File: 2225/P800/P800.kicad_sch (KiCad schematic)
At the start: 25 parts, among them J1 Screw_Terminal_01x04, J2 Screw_Terminal_01x08

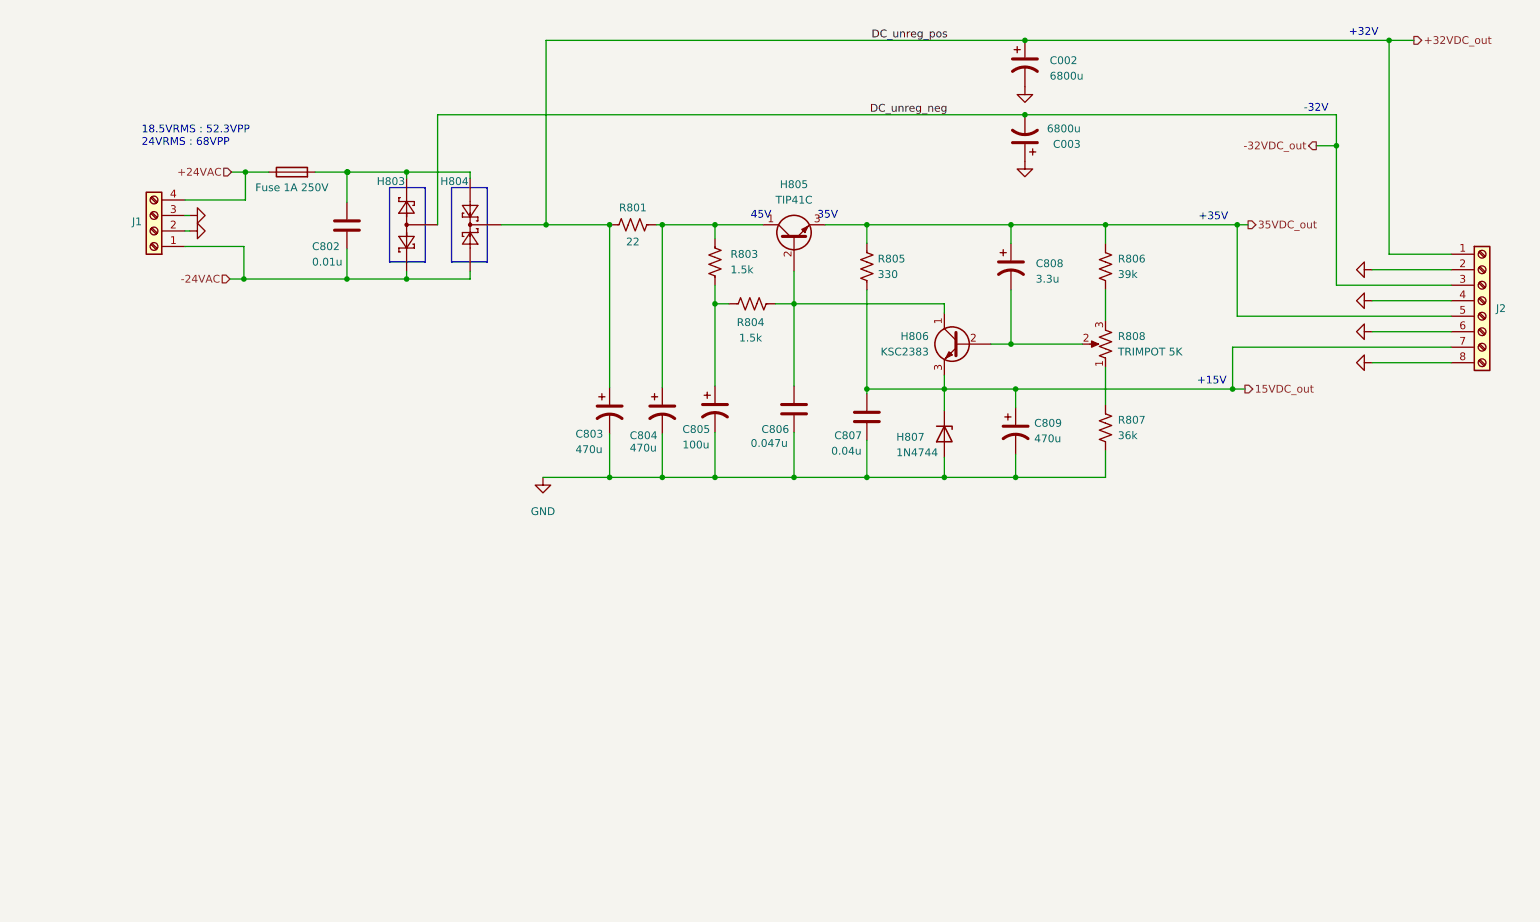
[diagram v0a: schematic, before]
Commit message: Connected transformer to P800 in 2225.kicad_sch; changed transformer model resistances in 2225.lib
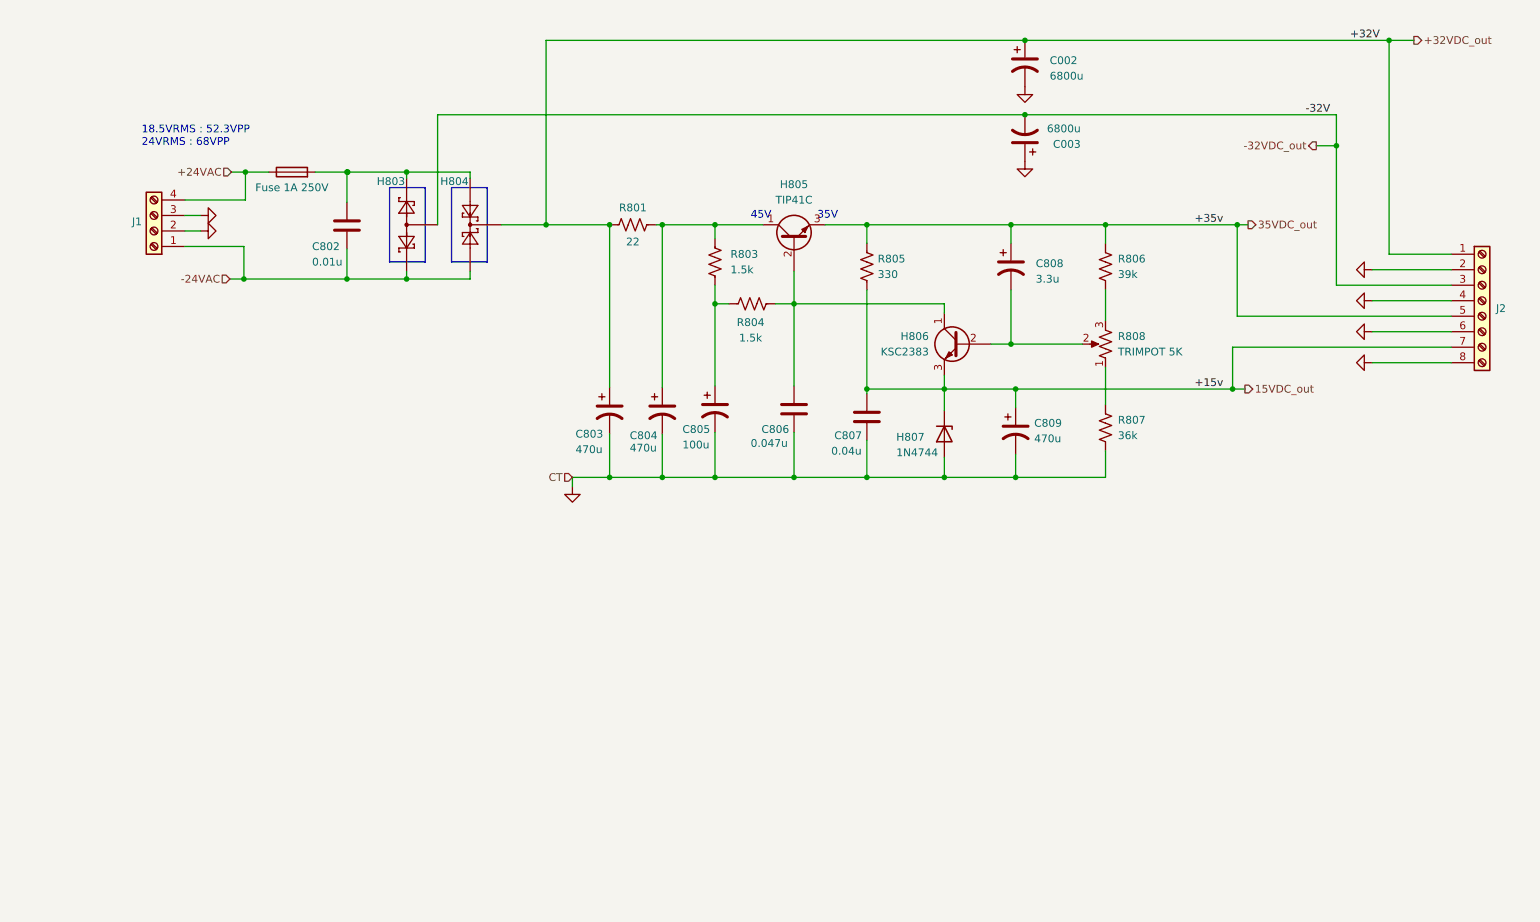
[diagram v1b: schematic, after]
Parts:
- J1: Spice_Model (none) -> Screw_Terminal_01x04; Spice_Netlist_Enabled (none) -> N; Spice_Primitive (none) -> J
- J2: Spice_Model (none) -> Screw_Terminal_01x08; Spice_Netlist_Enabled (none) -> N; Spice_Primitive (none) -> J
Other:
- note removed: "+15V"
- note removed: "+32V"
- note removed: "+35V"
- note removed: "-32V"
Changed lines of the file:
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@@
-    (stroke (width 0) (type default) (color 0 0 0 0))
-  )
-  (wire (pts (xy 102.362 125.222) (xy 113.284 125.222))
     (stroke (width 0) (type default) (color 0 0 0 0))
   )
@@
     (stroke (width 0) (type default) (color 0 0 0 0))
   )
-  (wire (pts (xy 44.45 84.836) (xy 43.688 84.836))
-    (stroke (width 0) (type default) (color 0 0 0 0))
-  )
   (polyline (pts (xy 83.058 77.724) (xy 83.058 89.916))
     (stroke (width 0) (type default) (color 0 0 0 0))
@@
     (stroke (width 0) (type default) (color 0 0 0 0))
   )
+  (wire (pts (xy 107.188 126.746) (xy 107.188 125.222))
+    (stroke (width 0) (type default) (color 0 0 0 0))
+  )
   (polyline (pts (xy 77.216 77.724) (xy 83.058 77.724))
     (stroke (width 0) (type default) (color 0 0 0 0))
@@
     (stroke (width 0) (type default) (color 0 0 0 0))
   )
-  (wire (pts (xy 44.45 82.296) (xy 43.688 82.296))
-    (stroke (width 0) (type default) (color 0 0 0 0))
-  )
   (wire (pts (xy 168.148 108.458) (xy 168.148 110.744))
     (stroke (width 0) (type default) (color 0 0 0 0))
@@
     (stroke (width 0) (type default) (color 0 0 0 0))
   )
+  (wire (pts (xy 46.228 84.836) (xy 43.688 84.836))
+    (stroke (width 0) (type default) (color 0 0 0 0))
+  )
   (wire (pts (xy 80.01 76.2) (xy 80.01 75.184))
     (stroke (width 0) (type default) (color 0 0 0 0))
@@
     (stroke (width 0) (type default) (color 0 0 0 0))
   )
+  (wire (pts (xy 43.688 82.296) (xy 46.228 82.296))
+    (stroke (width 0) (type default) (color 0 0 0 0))
+  )
   (wire (pts (xy 251.206 96.266) (xy 238.252 96.266))
     (stroke (width 0) (type default) (color 0 0 0 0))
@@
   )
   (wire (pts (xy 121.92 125.222) (xy 113.284 125.222))
+    (stroke (width 0) (type default) (color 0 0 0 0))
+  )
+  (wire (pts (xy 107.188 125.222) (xy 113.284 125.222))
     (stroke (width 0) (type default) (color 0 0 0 0))
   )
@@
     (effects (font (size 1.27 1.27)) (justify left bottom))
   )
-  (text "+15V" (at 209.55 110.236 0)
-    (effects (font (size 1.27 1.27)) (justify left bottom))
-  )
-  (text "+35V" (at 209.804 83.312 0)
-    (effects (font (size 1.27 1.27)) (justify left bottom))
-  )
   (text "35V" (at 147.32 83.058 0)
     (effects (font (size 1.27 1.27)) (justify left bottom))
   )
-  (text "-32V" (at 227.076 65.532 0)
-    (effects (font (size 1.27 1.27)) (justify left bottom))
-  )
-  (text "+32V" (at 234.442 53.086 0)
-    (effects (font (size 1.27 1.27)) (justify left bottom))
-  )
-  (label "DC_unreg_neg" (at 155.956 65.786 0)
-    (effects (font (size 1.27 1.27)) (justify left bottom))
-  )
-  (label "DC_unreg_pos" (at 156.21 53.594 0)
-    (effects (font (size 1.27 1.27)) (justify left bottom))
+  (label "+35v" (at 213.868 83.82 180)
+    (effects (font (size 1.27 1.27)) (justify right bottom))
+  )
+  (label "-32V" (at 231.394 65.786 180)
+    (effects (font (size 1.27 1.27)) (justify right bottom))
+  )
+  (label "+32V" (at 239.522 53.594 180)
+    (effects (font (size 1.27 1.27)) (justify right bottom))
+  )
+  (label "+15v" (at 213.868 110.744 180)
+    (effects (font (size 1.27 1.27)) (justify right bottom))
   )
   (hierarchical_label "35VDC_out" (shape output) (at 217.932 83.82 0)
     (effects (font (size 1.27 1.27)) (justify left))
   )
+  (hierarchical_label "CT" (shape input) (at 107.188 125.222 180)
+    (effects (font (size 1.27 1.27)) (justify right))
+  )
   (hierarchical_label "-24VAC" (shape input) (at 51.054 92.71 180)
     (effects (font (size 1.27 1.27)) (justify right))
@@
     (pin "2")
   )
-  (symbol (lib_id "power:GND") (at 44.45 82.296 90) (unit 1)
-    (in_bom yes) (on_board yes) (fields_autoplaced)
-    (property "Reference" "#PWR?" (id 0) (at 50.8 82.296 0)
-      (effects (font (size 1.27 1.27)) hide)
-    )
-    (property "Value" "GND" (id 1) (at 47.752 82.2959 90)
-      (effects (font (size 1.27 1.27)) (justify right) hide)
-    )
-    (property "Footprint" "" (id 2) (at 44.45 82.296 0)
-      (effects (font (size 1.27 1.27)) hide)
-    )
-    (property "Datasheet" "" (id 3) (at 44.45 82.296 0)
-      (effects (font (size 1.27 1.27)) hide)
-    )
-    (pin "1")
-  )
   (symbol (lib_id "Device:R_US") (at 194.564 90.678 180) (unit 1)
     (in_bom yes) (on_board yes) (fields_autoplaced)
@@
     )
     (property "Datasheet" "~" (id 3) (at 256.286 96.266 0)
+      (effects (font (size 1.27 1.27)) hide)
+    )
+    (property "Spice_Primitive" "J" (id 4) (at 256.286 96.266 0)
+      (effects (font (size 1.27 1.27)) hide)
+    )
+    (property "Spice_Model" "Screw_Terminal_01x08" (id 5) (at 256.286 96.266 0)
+      (effects (font (size 1.27 1.27)) hide)
+    )
+    (property "Spice_Netlist_Enabled" "N" (id 6) (at 256.286 96.266 0)
       (effects (font (size 1.27 1.27)) hide)
     )
@@
     (pin "8")
   )
-  (symbol (lib_id "power:GND") (at 102.362 125.222 0) (unit 1)
-    (in_bom yes) (on_board yes) (fields_autoplaced)
-    (property "Reference" "#PWR?" (id 0) (at 102.362 131.572 0)
-      (effects (font (size 1.27 1.27)) hide)
-    )
-    (property "Value" "GND" (id 1) (at 102.362 130.81 0))
-    (property "Footprint" "" (id 2) (at 102.362 125.222 0)
-      (effects (font (size 1.27 1.27)) hide)
-    )
-    (property "Datasheet" "" (id 3) (at 102.362 125.222 0)
-      (effects (font (size 1.27 1.27)) hide)
-    )
-    (pin "1")
-  )
   (symbol (lib_id "power:GND") (at 238.252 91.186 270) (unit 1)
     (in_bom yes) (on_board yes) (fields_autoplaced)
@@
     (pin "3")
   )
+  (symbol (lib_id "power:GND") (at 107.188 126.746 0) (unit 1)
+    (in_bom yes) (on_board yes) (fields_autoplaced)
+    (property "Reference" "#PWR?" (id 0) (at 107.188 133.096 0)
+      (effects (font (size 1.27 1.27)) hide)
+    )
+    (property "Value" "GND" (id 1) (at 107.1881 130.048 90)
+      (effects (font (size 1.27 1.27)) (justify right) hide)
+    )
+    (property "Footprint" "" (id 2) (at 107.188 126.746 0)
+      (effects (font (size 1.27 1.27)) hide)
+    )
+    (property "Datasheet" "" (id 3) (at 107.188 126.746 0)
+      (effects (font (size 1.27 1.27)) hide)
+    )
+    (pin "1")
+  )
   (symbol (lib_id "power:GND") (at 238.252 106.426 270) (unit 1)
     (in_bom yes) (on_board yes) (fields_autoplaced)
@@
     (pin "2")
   )
+  (symbol (lib_id "power:GND") (at 46.228 84.836 90) (unit 1)
+    (in_bom yes) (on_board yes) (fields_autoplaced)
+    (property "Reference" "#PWR?" (id 0) (at 52.578 84.836 0)
+      (effects (font (size 1.27 1.27)) hide)
+    )
+    (property "Value" "GND" (id 1) (at 49.53 84.8359 90)
+      (effects (font (size 1.27 1.27)) (justify right) hide)
+    )
+    (property "Footprint" "" (id 2) (at 46.228 84.836 0)
+      (effects (font (size 1.27 1.27)) hide)
+    )
+    (property "Datasheet" "" (id 3) (at 46.228 84.836 0)
+      (effects (font (size 1.27 1.27)) hide)
+    )
+    (pin "1")
+  )
   (symbol (lib_id "Device:C_Polarized_US") (at 113.284 114.3 0) (unit 1)
     (in_bom yes) (on_board yes)
@@
     (pin "1")
     (pin "2")
-  )
-  (symbol (lib_id "power:GND") (at 44.45 84.836 90) (unit 1)
-    (in_bom yes) (on_board yes) (fields_autoplaced)
-    (property "Reference" "#PWR?" (id 0) (at 50.8 84.836 0)
-      (effects (font (size 1.27 1.27)) hide)
-    )
-    (property "Value" "GND" (id 1) (at 47.752 84.8359 90)
-      (effects (font (size 1.27 1.27)) (justify right) hide)
-    )
-    (property "Footprint" "" (id 2) (at 44.45 84.836 0)
-      (effects (font (size 1.27 1.27)) hide)
-    )
-    (property "Datasheet" "" (id 3) (at 44.45 84.836 0)
-      (effects (font (size 1.27 1.27)) hide)
-    )
-    (pin "1")
   )
   (symbol (lib_id "Device:R_US") (at 136.652 96.774 270) (unit 1)
@@
     (pin "2")
   )
+  (symbol (lib_id "power:GND") (at 46.228 82.296 90) (unit 1)
+    (in_bom yes) (on_board yes) (fields_autoplaced)
+    (property "Reference" "#PWR?" (id 0) (at 52.578 82.296 0)
+      (effects (font (size 1.27 1.27)) hide)
+    )
+    (property "Value" "GND" (id 1) (at 49.53 82.2959 90)
+      (effects (font (size 1.27 1.27)) (justify right) hide)
+    )
+    (property "Footprint" "" (id 2) (at 46.228 82.296 0)
+      (effects (font (size 1.27 1.27)) hide)
+    )
+    (property "Datasheet" "" (id 3) (at 46.228 82.296 0)
+      (effects (font (size 1.27 1.27)) hide)
+    )
+    (pin "1")
+  )
   (symbol (lib_id "Device:R_US") (at 117.094 83.82 90) (unit 1)
     (in_bom yes) (on_board yes)
@@
       (effects (font (size 1.27 1.27)) hide)
     )
+    (property "Spice_Primitive" "J" (id 4) (at 38.608 84.836 0)
+      (effects (font (size 1.27 1.27)) hide)
+    )
+    (property "Spice_Model" "Screw_Terminal_01x04" (id 5) (at 38.608 84.836 0)
+      (effects (font (size 1.27 1.27)) hide)
+    )
+    (property "Spice_Netlist_Enabled" "N" (id 6) (at 38.608 84.836 0)
+      (effects (font (size 1.27 1.27)) hide)
+    )

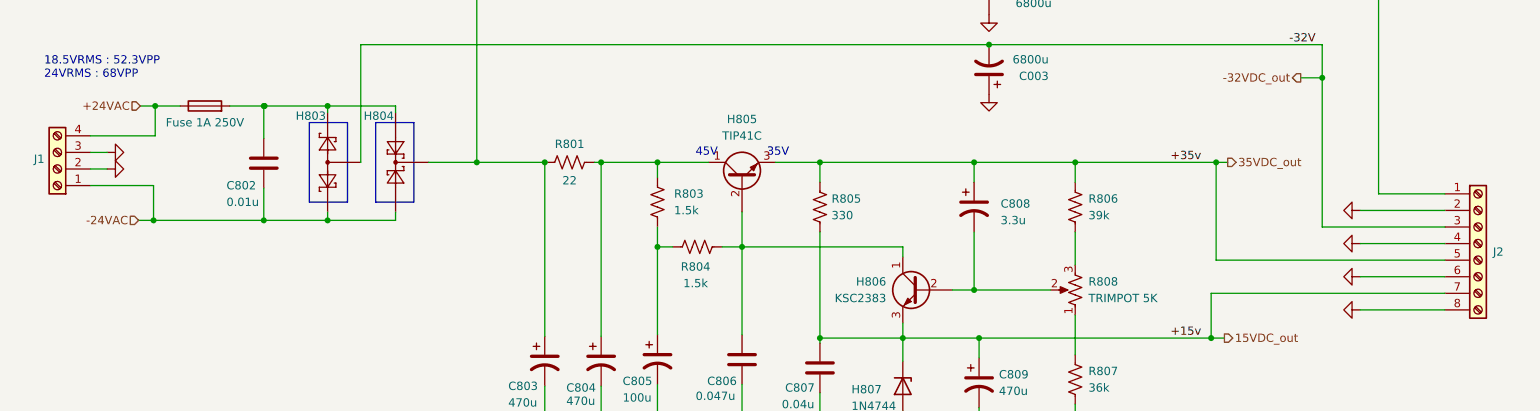
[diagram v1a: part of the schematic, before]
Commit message: Connected P800 (DC supply) to PE01 tone board, audio source to PE01, and PE01 to dummy P700 main amplifier. Changed some hierarchical label names in multiple schematics.
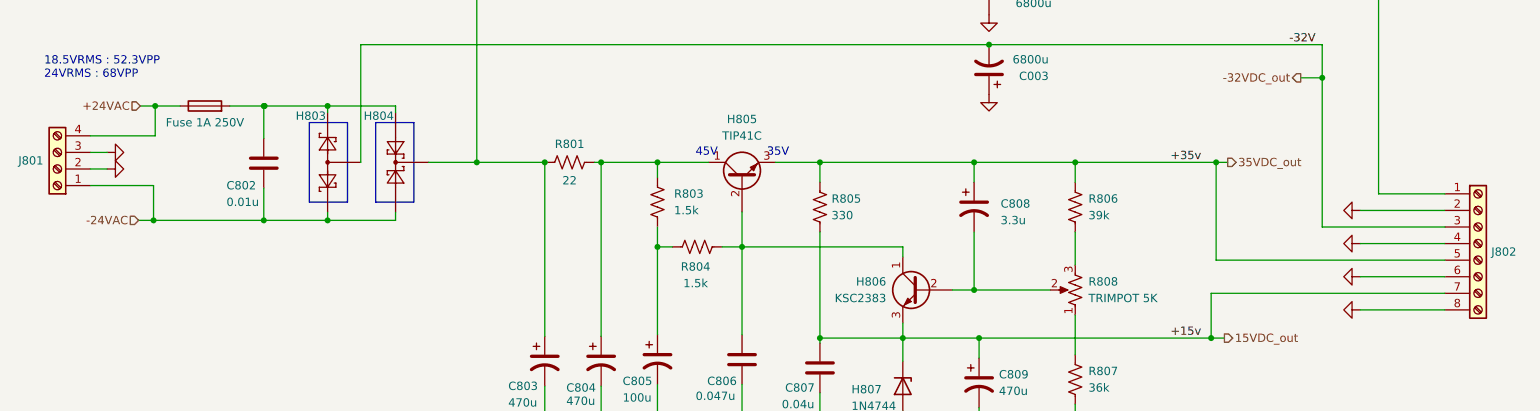
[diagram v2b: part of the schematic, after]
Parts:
- renumbered J1 to J801, J2 to J802
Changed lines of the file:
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@@
   )
   (symbol (lib_id "Connector:Screw_Terminal_01x08") (at 256.286 96.266 0) (unit 1)
-    (in_bom yes) (on_board yes) (fields_autoplaced)
-    (property "Reference" "J2" (id 0) (at 258.572 97.5359 0)
+    (in_bom yes) (on_board yes)
+    (property "Reference" "J802" (id 0) (at 258.318 97.536 0)
       (effects (font (size 1.27 1.27)) (justify left))
     )
@@
   (symbol (lib_id "power:GND") (at 238.252 91.186 270) (unit 1)
     (in_bom yes) (on_board yes) (fields_autoplaced)
-    (property "Reference" "#PWR?" (id 0) (at 231.902 91.186 0)
+    (property "Reference" "#PWR0105" (id 0) (at 231.902 91.186 0)
       (effects (font (size 1.27 1.27)) hide)
     )
@@
   (symbol (lib_id "power:GND") (at 238.252 101.346 270) (unit 1)
     (in_bom yes) (on_board yes) (fields_autoplaced)
-    (property "Reference" "#PWR?" (id 0) (at 231.902 101.346 0)
+    (property "Reference" "#PWR0106" (id 0) (at 231.902 101.346 0)
       (effects (font (size 1.27 1.27)) hide)
     )
@@
   (symbol (lib_id "power:GND") (at 107.188 126.746 0) (unit 1)
     (in_bom yes) (on_board yes) (fields_autoplaced)
-    (property "Reference" "#PWR?" (id 0) (at 107.188 133.096 0)
+    (property "Reference" "#PWR0102" (id 0) (at 107.188 133.096 0)
       (effects (font (size 1.27 1.27)) hide)
     )
@@
   (symbol (lib_id "power:GND") (at 238.252 106.426 270) (unit 1)
     (in_bom yes) (on_board yes) (fields_autoplaced)
-    (property "Reference" "#PWR?" (id 0) (at 231.902 106.426 0)
+    (property "Reference" "#PWR0111" (id 0) (at 231.902 106.426 0)
       (effects (font (size 1.27 1.27)) hide)
     )
@@
   (symbol (lib_id "power:GND") (at 181.356 73.406 0) (unit 1)
     (in_bom yes) (on_board yes) (fields_autoplaced)
-    (property "Reference" "#PWR?" (id 0) (at 181.356 79.756 0)
+    (property "Reference" "#PWR0103" (id 0) (at 181.356 79.756 0)
       (effects (font (size 1.27 1.27)) hide)
     )
@@
   (symbol (lib_id "power:GND") (at 46.228 84.836 90) (unit 1)
     (in_bom yes) (on_board yes) (fields_autoplaced)
-    (property "Reference" "#PWR?" (id 0) (at 52.578 84.836 0)
+    (property "Reference" "#PWR0112" (id 0) (at 52.578 84.836 0)
       (effects (font (size 1.27 1.27)) hide)
     )
@@
   (symbol (lib_id "power:GND") (at 238.252 96.266 270) (unit 1)
     (in_bom yes) (on_board yes) (fields_autoplaced)
-    (property "Reference" "#PWR?" (id 0) (at 231.902 96.266 0)
+    (property "Reference" "#PWR0110" (id 0) (at 231.902 96.266 0)
       (effects (font (size 1.27 1.27)) hide)
     )
@@
   (symbol (lib_id "power:GND") (at 46.228 82.296 90) (unit 1)
     (in_bom yes) (on_board yes) (fields_autoplaced)
-    (property "Reference" "#PWR?" (id 0) (at 52.578 82.296 0)
+    (property "Reference" "#PWR0113" (id 0) (at 52.578 82.296 0)
       (effects (font (size 1.27 1.27)) hide)
     )
@@
   (symbol (lib_id "power:GND") (at 181.356 61.214 0) (unit 1)
     (in_bom yes) (on_board yes) (fields_autoplaced)
-    (property "Reference" "#PWR?" (id 0) (at 181.356 67.564 0)
+    (property "Reference" "#PWR0104" (id 0) (at 181.356 67.564 0)
       (effects (font (size 1.27 1.27)) hide)
     )
@@
   (symbol (lib_id "Connector:Screw_Terminal_01x04") (at 38.608 84.836 180) (unit 1)
     (in_bom yes) (on_board yes)
-    (property "Reference" "J1" (id 0) (at 35.814 83.312 0))
+    (property "Reference" "J801" (id 0) (at 34.544 83.566 0))
     (property "Value" "Screw_Terminal_01x04" (id 1) (at 38.608 75.692 0)
       (effects (font (size 1.27 1.27)) hide)
